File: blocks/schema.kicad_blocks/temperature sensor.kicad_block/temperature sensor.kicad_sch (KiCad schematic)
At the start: 4 parts, among them U11 MCP9701A

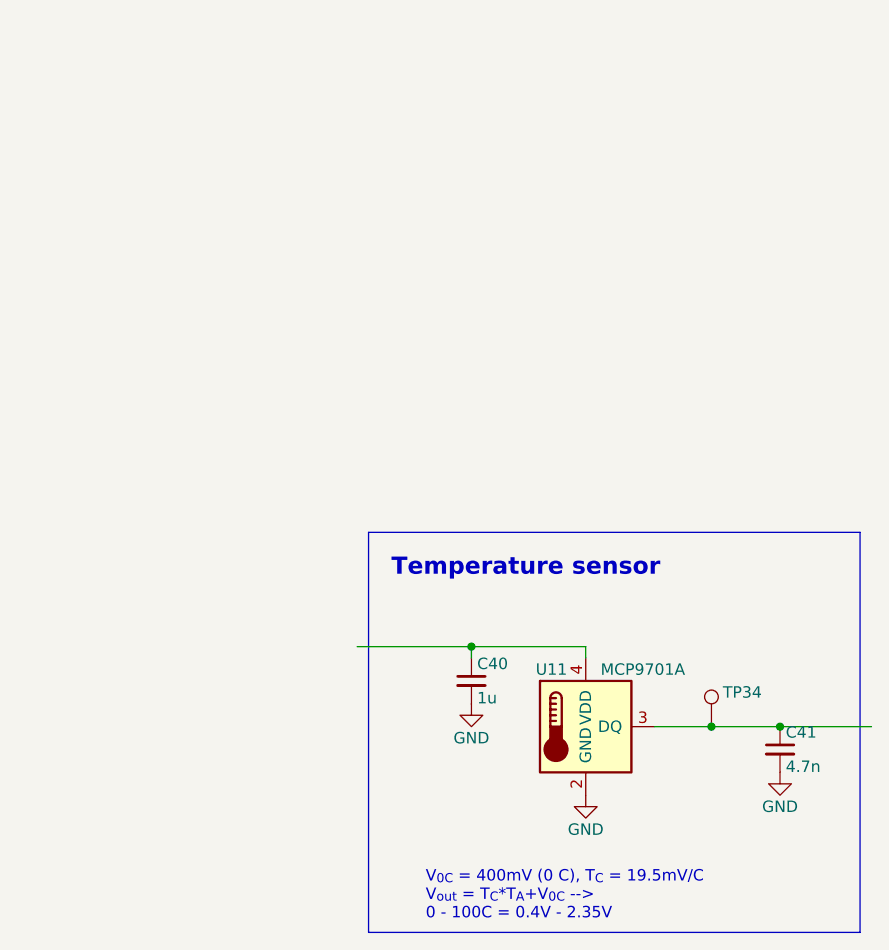
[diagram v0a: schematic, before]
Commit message: Add some components+footprints
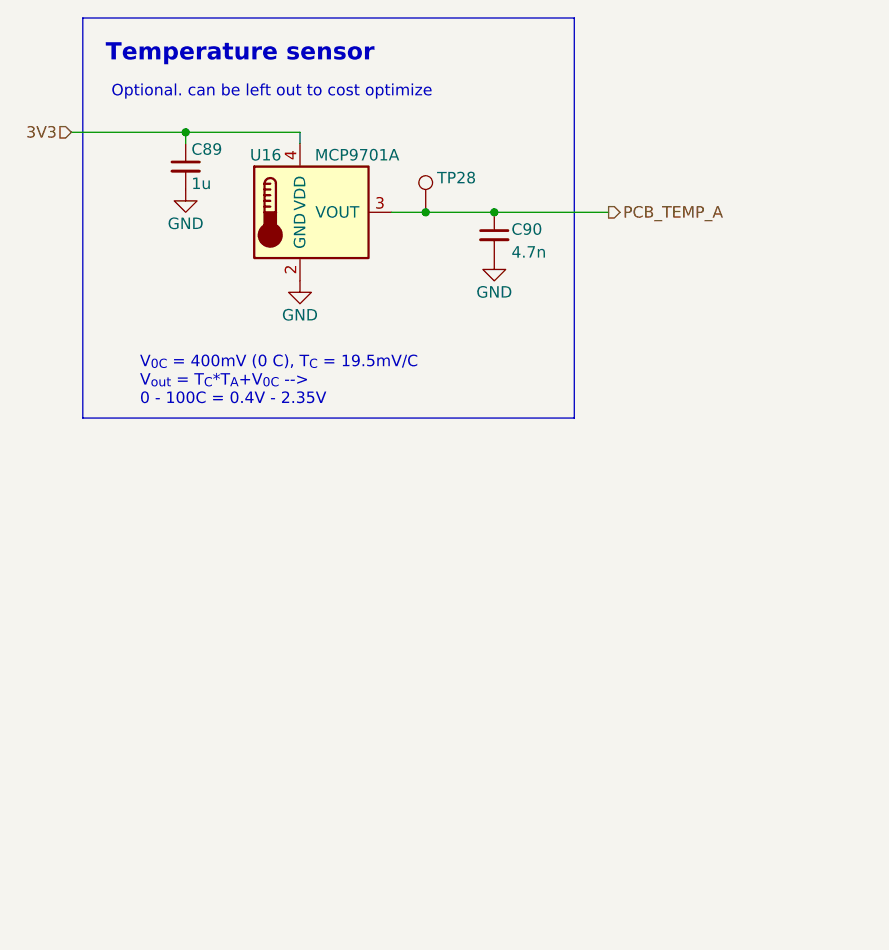
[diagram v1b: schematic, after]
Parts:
- C90: renamed from C41; rating (none) -> X7R, 50V
- TP28: renamed from TP34; footprint TestPoint:TestPoint_THTPad_D1.0mm_Drill0.5mm -> TestPoint:TestPoint_Pad_D1.0mm
- renumbered C40 to C89, U11 to U16
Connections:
- net PCB_TEMP_A: now reaches C90.1, TP28.1, U16.3 (VOUT)
- net 3V3: now reaches C89.1, U16.4 (VDD)
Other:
- note added: "Optional. can be left out to cost optimize"
- title: (none) -> PCB temperature sensor
- moved on the sheet: C89, C90, TP28, U16
